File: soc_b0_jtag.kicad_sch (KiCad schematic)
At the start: 37 parts, among them J20 Conn_02x07_Odd_Even, J21 Conn_ARM_SWD_TagConnect_TC2050, J22 Conn_01x02, Q11 BSS138, SW3 SW_Push, U21 XC7Z030_FBG676, U22 SN74LXC1T45DBVR

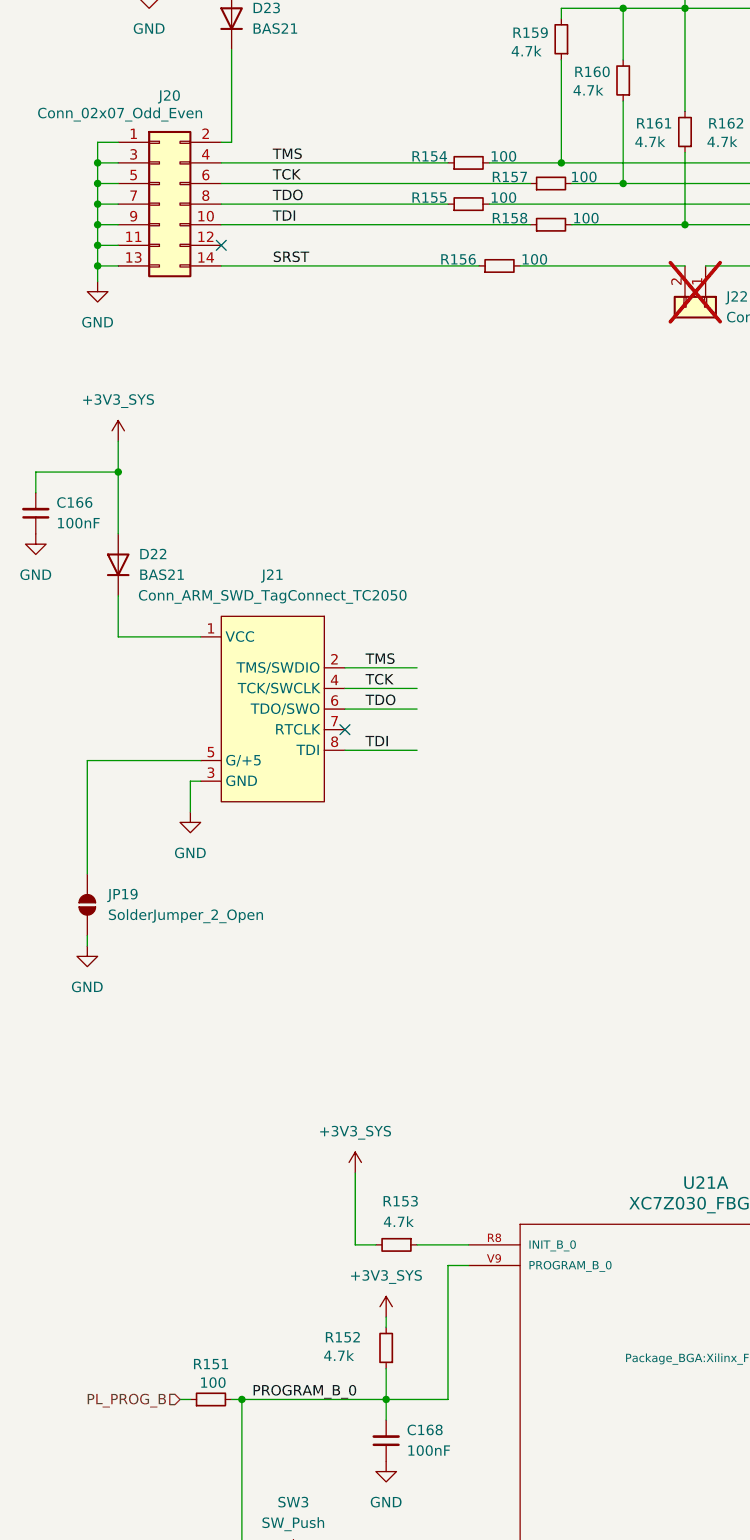
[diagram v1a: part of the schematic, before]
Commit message: schema: JTAG connector & resistors, rev change
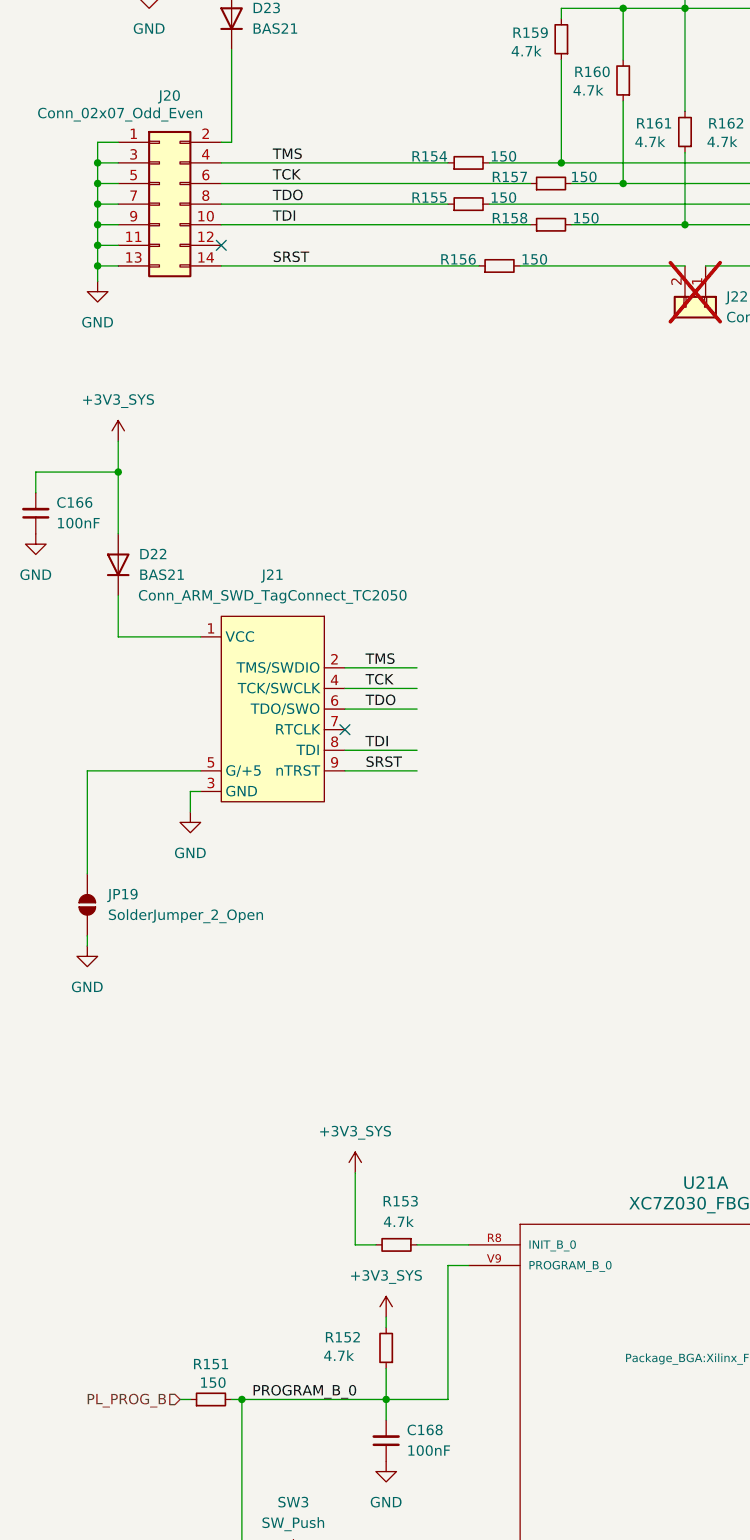
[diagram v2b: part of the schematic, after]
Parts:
- R151, R154, R155, R156, R157, R158: value 100 -> 150; JLCPCB Part # C153111 -> C25082; Part RM04FTN1000 -> 0402WGF1500TCE
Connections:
- net SRST: now also J21.9 (nTRST)
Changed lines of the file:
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@@
 		(title "NASR-M")
 		(date "2025-10-22")
-		(rev "D 0.9.5")
+		(rev "D 0.9.8")
 		(company "electrodyssey.net")
 		(comment 1 "JTAG / PS reset / PL reset ")
@@
 		(comment 3 "Author: Nazim Aghabayov")
 		(comment 4 "SYZYGY Carrier Mainboard")
-		(comment 5 "rel: Fletched Bustard")
+		(comment 5 "rel: Wild Goose")
 	)
 	(junction
@@
 	(wire
 		(pts
-			(xy 22.86 129.54) (xy 22.86 143.51)
+			(xy 22.86 130.81) (xy 22.86 143.51)
 		)
 		(stroke
@@
 	(wire
 		(pts
-			(xy 35.56 132.08) (xy 36.83 132.08)
+			(xy 35.56 133.35) (xy 36.83 133.35)
 		)
 		(stroke
@@
 	(wire
 		(pts
+			(xy 54.61 130.81) (xy 63.5 130.81)
+		)
+		(stroke
+			(width 0)
+			(type default)
+		)
+	)
+	(wire
+		(pts
 			(xy 128.27 212.09) (xy 138.43 212.09)
 		)
@@
 	(wire
 		(pts
-			(xy 35.56 132.08) (xy 35.56 135.89)
+			(xy 35.56 133.35) (xy 35.56 135.89)
 		)
 		(stroke
@@
 	(wire
 		(pts
-			(xy 36.83 129.54) (xy 22.86 129.54)
+			(xy 36.83 130.81) (xy 22.86 130.81)
 		)
 		(stroke
@@
 		)
 	)
+	(label "SRST"
+		(at 57.15 130.81 0)
+		(effects
+			(font
+				(size 1.27 1.27)
+			)
+			(justify left bottom)
+		)
+	)
 	(label "TMS"
 		(at 45.72 55.88 0)
@@
 			)
 		)
-		(property "Value" "100"
+		(property "Value" "150"
 			(at 74.168 55.118 90)
 			(effects
@@
 			)
 		)
-		(property "JLCPCB Part #" "C153111"
+		(property "JLCPCB Part #" "C25082"
 			(at 69.85 55.88 0)
 			(effects
@@
 			)
 		)
-		(property "Part" "RM04FTN1000"
+		(property "Part" "0402WGF1500TCE"
 			(at 69.85 55.88 90)
 			(effects
@@
 			)
 		)
-		(property "Value" "100"
+		(property "Value" "150"
 			(at 74.168 60.198 90)
 			(effects
@@
 			)
 		)
-		(property "JLCPCB Part #" "C153111"
+		(property "JLCPCB Part #" "C25082"
 			(at 69.85 60.96 0)
 			(effects
@@
 			)
 		)
-		(property "Part" "RM04FTN1000"
+		(property "Part" "0402WGF1500TCE"
 			(at 69.85 60.96 90)
 			(effects
@@
 			)
 		)
-		(property "Value" "100"
+		(property "Value" "150"
 			(at 84.328 62.738 90)
 			(effects
@@
 			)
 		)
-		(property "JLCPCB Part #" "C153111"
+		(property "JLCPCB Part #" "C25082"
 			(at 80.01 63.5 0)
 			(effects
@@
 			)
 		)
-		(property "Part" "RM04FTN1000"
+		(property "Part" "0402WGF1500TCE"
 			(at 80.01 63.5 90)
 			(effects
@@
 			)
 		)
-		(property "Value" "100"
+		(property "Value" "150"
 			(at 84.074 57.658 90)
 			(effects
@@
 			)
 		)
-		(property "JLCPCB Part #" "C153111"
+		(property "JLCPCB Part #" "C25082"
 			(at 80.01 58.42 0)
 			(effects
@@
 			)
 		)
-		(property "Part" "RM04FTN1000"
+		(property "Part" "0402WGF1500TCE"
 			(at 80.01 58.42 90)
 			(effects
@@
 			)
 		)
-		(property "Value" "100"
+		(property "Value" "150"
 			(at 38.354 206.248 90)
 			(effects
@@
 			)
 		)
-		(property "JLCPCB Part #" "C153111"
+		(property "JLCPCB Part #" "C25082"
 			(at 38.1 208.28 0)
 			(effects
@@
 			)
 		)
-		(property "Part" "RM04FTN1000"
+		(property "Part" "0402WGF1500TCE"
 			(at 38.1 208.28 90)
 			(effects
@@
 			)
 		)
-		(property "Value" "100"
+		(property "Value" "150"
 			(at 77.978 67.818 90)
 			(effects
@@
 			)
 		)
-		(property "JLCPCB Part #" "C153111"
+		(property "JLCPCB Part #" "C25082"
 			(at 73.66 68.58 0)
 			(effects
@@
 			)
 		)
-		(property "Part" "RM04FTN1000"
+		(property "Part" "0402WGF1500TCE"
 			(at 73.66 68.58 90)
 			(effects
@@
 		(pin "2"
 		)
+		(pin "9"
+		)
 		(instances
